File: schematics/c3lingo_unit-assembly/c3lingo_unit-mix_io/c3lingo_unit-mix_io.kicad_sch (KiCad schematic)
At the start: 42 parts, among them J201 Stage Line-In, J202 Mix Line-Out, J203 PowerSupply, J204 Inputs, J205 Output, U201 LM833N, U202 DRV134PA, U203 LM833N

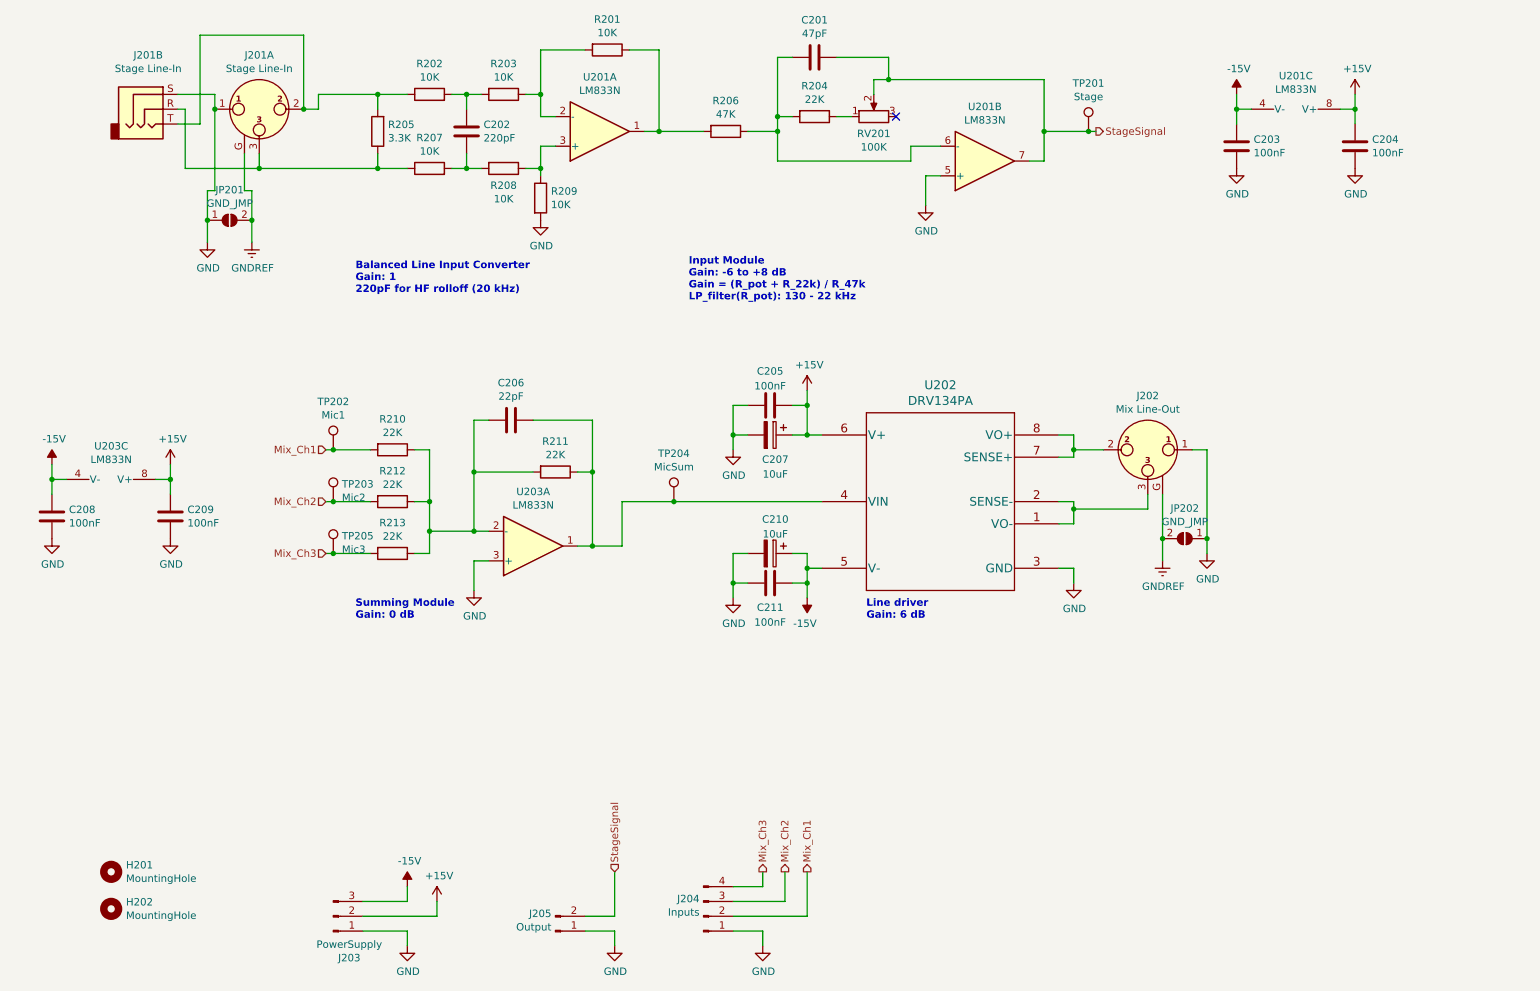
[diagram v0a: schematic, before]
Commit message: Reworks board-to-board connections
Instead of having connections between all boards, use the mix_io board as an audio signal distribution hub.

Note: PCB not updated
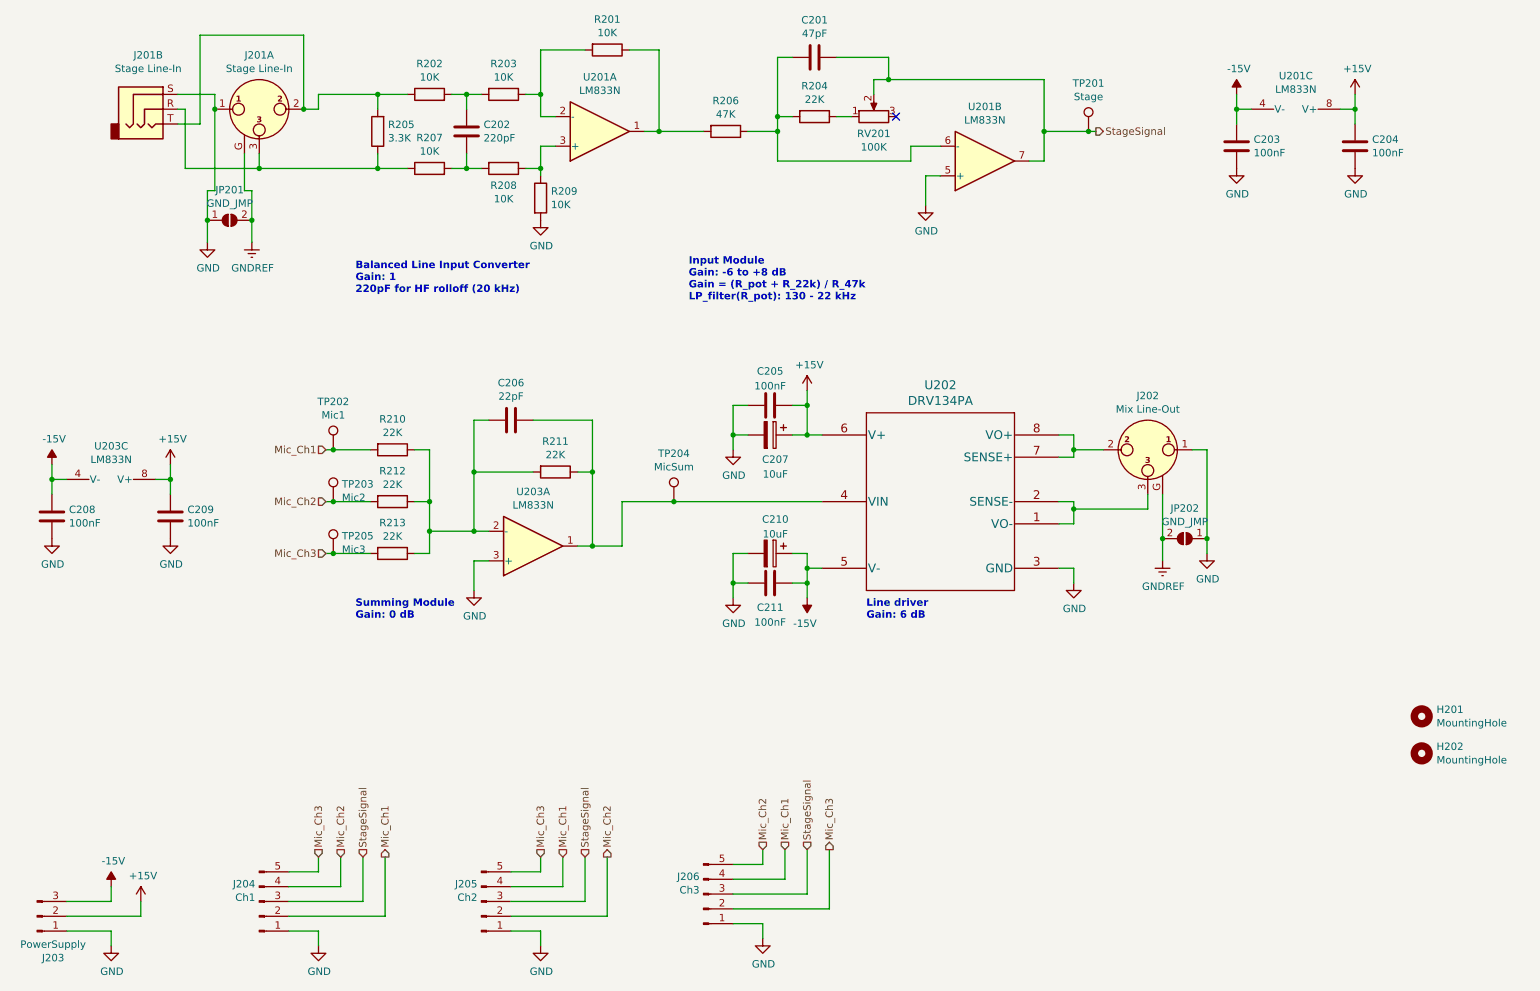
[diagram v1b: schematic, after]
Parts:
- removed J205: Output, TerminalBlock_Phoenix:TerminalBlock_Phoenix_PTSM-0,5-2-2.5-V-THR_1x02_P2.50mm_Vertical, symbol Connector:Conn_01x02_Pin
- added J205: Ch2, TerminalBlock_Phoenix:TerminalBlock_Phoenix_PTSM-0,5-5-2.5-V-THR_1x05_P2.50mm_Vertical, symbol Connector:Conn_01x05_Pin
- added J206: Ch3, TerminalBlock_Phoenix:TerminalBlock_Phoenix_PTSM-0,5-5-2.5-V-THR_1x05_P2.50mm_Vertical, symbol Connector:Conn_01x05_Pin
- J203: footprint TerminalBlock_Phoenix:TerminalBlock_Phoenix_PTSM-0,5-3-2.5-H-THR_1x03_P2.50mm_Horizontal -> TerminalBlock_Phoenix:TerminalBlock_Phoenix_PTSM-0,5-3-2.5-V-THR_1x03_P2.50mm_Vertical
- J204: value Inputs -> Ch1; footprint TerminalBlock_Phoenix:TerminalBlock_Phoenix_PTSM-0,5-4-2.5-V-THR_1x04_P2.50mm_Vertical -> TerminalBlock_Phoenix:TerminalBlock_Phoenix_PTSM-0,5-5-2.5-V-THR_1x05_P2.50mm_Vertical; symbol Connector:Conn_01x04_Pin -> Connector:Conn_01x05_Pin; Model PTSM 0,5/ 4-2,5-V THR -> PTSM 0,5/ 5-2,5-V THR
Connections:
- net GND: now also J205.1 (Pin_1), J206.1 (Pin_1)
- net StageSignal: now also J204.3 (Pin_3), J205.3 (Pin_3), J206.3 (Pin_3)
- net Mix_Ch1 renamed Mic_Ch1
- net Mic_Ch1: now also J205.4 (Pin_4), J206.4 (Pin_4)
- net Mix_Ch2 renamed Mic_Ch2
- net Mic_Ch2: now also J204.4 (Pin_4), J205.2 (Pin_2), J206.5 (Pin_5); no longer J204.3 (Pin_3)
- net Mix_Ch3 renamed Mic_Ch3
- net Mic_Ch3: now also J204.5 (Pin_5), J205.5 (Pin_5), J206.2 (Pin_2); no longer J204.4 (Pin_4)
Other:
- moved on the sheet: H201, H202, J203

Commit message: Re-layout boards with SMD components
* Channel Mix: Removed vu meter potentiometer as good setting was found (10 dB
  more headroom)
* Channel Mix: Add vu meter alternate power
* Channel I/O: Added jumper for phantom power enable/disable
* Add GND test points
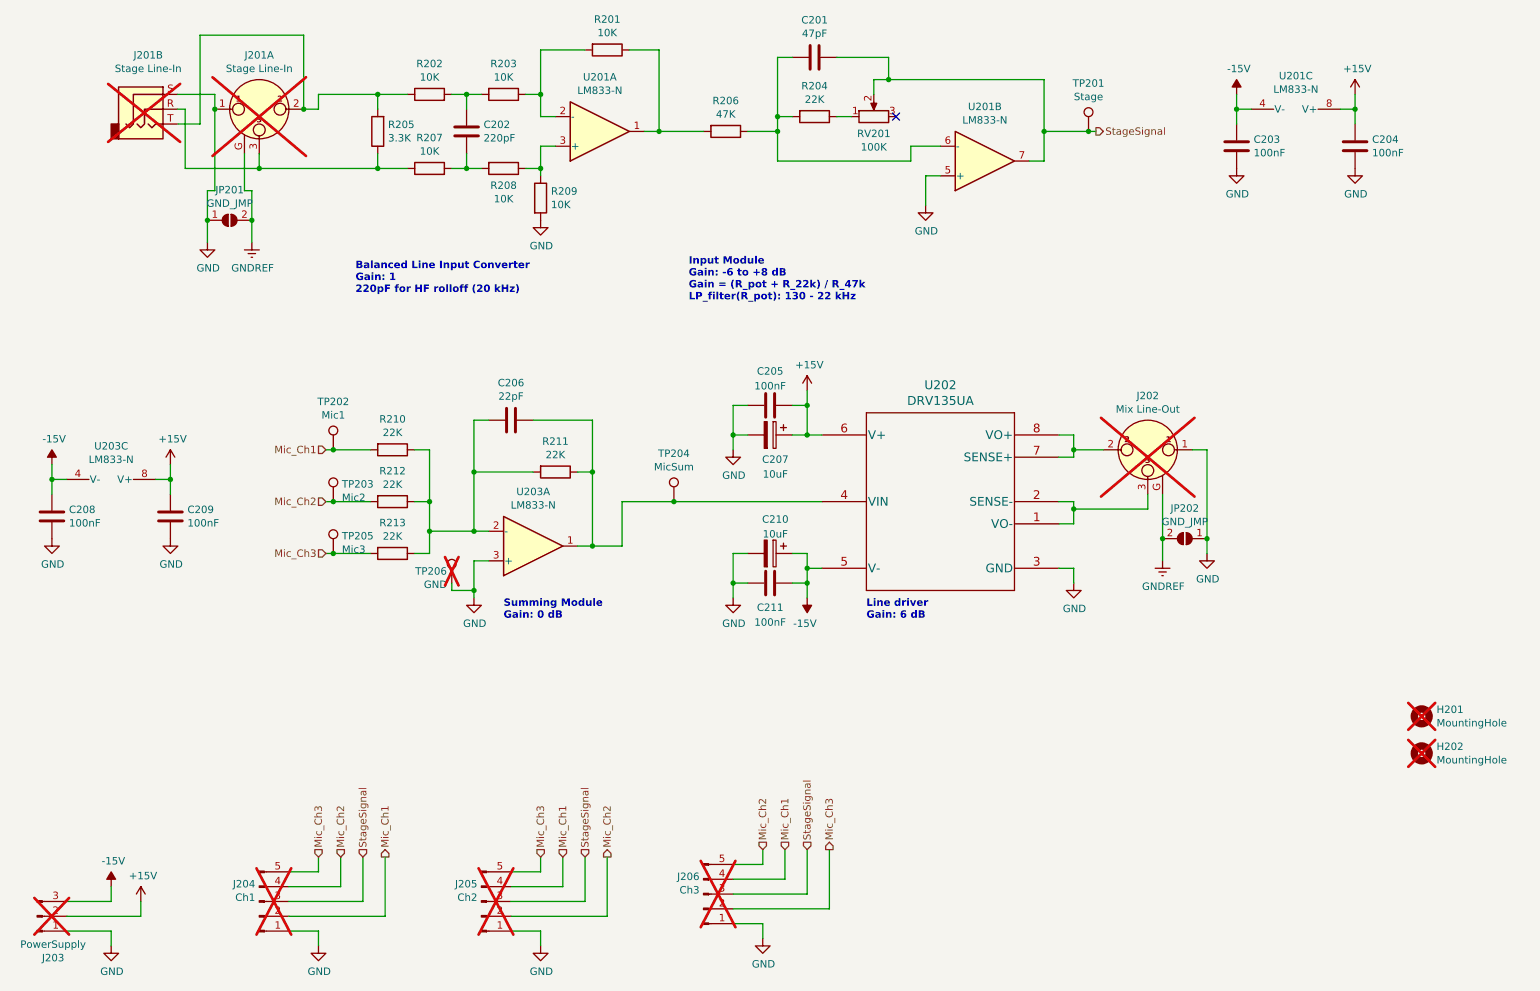
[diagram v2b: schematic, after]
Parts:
- added TP206: GND, TestPoint:TestPoint_Keystone_5005-5009_Compact, symbol Connector:TestPoint
- C201: footprint Capacitor_THT:C_Disc_D5.0mm_W2.5mm_P5.00mm -> Capacitor_SMD:C_0603_1608Metric_Pad1.08x0.95mm_HandSolder; LCSC Part # (none) -> C1671; Model (none) -> 5% C0G
- C202: footprint Capacitor_THT:C_Disc_D5.0mm_W2.5mm_P5.00mm -> Capacitor_SMD:C_0603_1608Metric_Pad1.08x0.95mm_HandSolder; LCSC Part # (none) -> C1603; Model (none) -> 5% C0G
- C203, C204, C205, C208, C209, C211: footprint Capacitor_THT:C_Disc_D5.0mm_W2.5mm_P5.00mm -> Capacitor_SMD:C_0603_1608Metric_Pad1.08x0.95mm_HandSolder; LCSC Part # (none) -> C14663; Model (none) -> 10% X7R 25V+
- C206: footprint Capacitor_THT:C_Disc_D5.0mm_W2.5mm_P5.00mm -> Capacitor_SMD:C_0603_1608Metric_Pad1.08x0.95mm_HandSolder; LCSC Part # (none) -> C1653; Model (none) -> 5% C0G
- C207, C210: footprint Capacitor_THT:CP_Radial_D5.0mm_P2.00mm -> Capacitor_SMD:C_Elec_4x5.4; LCSC Part # (none) -> C3001226; Model (none) -> 25V+
- H201, H202: now not fitted; now left out of the parts list
- J201, J202, J204, J205, J206: now not fitted
- J203: Model PTSM 0,5/ 3-2,5-H THR -> PTSM 0,5/ 3-2,5-V THR; now not fitted
- JP201, JP202, TP201, TP202, TP203, TP204, TP205: now left out of the parts list
- R201, R202, R203, R207, R208, R209: footprint Resistor_THT:R_Axial_DIN0207_L6.3mm_D2.5mm_P10.16mm_Horizontal -> Resistor_SMD:R_0805_2012Metric_Pad1.20x1.40mm_HandSolder; LCSC Part # (none) -> C17414
- R204, R210, R211, R212, R213: footprint Resistor_THT:R_Axial_DIN0207_L6.3mm_D2.5mm_P10.16mm_Horizontal -> Resistor_SMD:R_0805_2012Metric_Pad1.20x1.40mm_HandSolder; LCSC Part # (none) -> C17560
- R205: footprint Resistor_THT:R_Axial_DIN0207_L6.3mm_D2.5mm_P10.16mm_Horizontal -> Resistor_SMD:R_0805_2012Metric_Pad1.20x1.40mm_HandSolder; LCSC Part # (none) -> C26010
- R206: footprint Resistor_THT:R_Axial_DIN0207_L6.3mm_D2.5mm_P10.16mm_Horizontal -> Resistor_SMD:R_0805_2012Metric_Pad1.20x1.40mm_HandSolder; LCSC Part # (none) -> C17713
- RV201: Model Vishay M64Y104 -> Bourns PV36Y104C01B00 or Vishay M64Y104
- U201, U203: value LM833N -> LM833-N; footprint Package_DIP:DIP-8_W7.62mm_Socket_LongPads -> Package_SO:SOIC-8_3.9x4.9mm_P1.27mm; LCSC Part # (none) -> C473907; Model +DIP-8 Socket -> LM833M or LM833MX (SOIC-8)
- U202: value DRV134PA -> DRV135UA; footprint Package_DIP:DIP-8_W7.62mm -> Package_SO:SOIC-8_3.9x4.9mm_P1.27mm; symbol JBeyerstedt-Library:DRV134PA -> c3lingo_unit:DRV134PA; LCSC Part # (none) -> C431073; Model +DIP-8 Socket -> DRV135UA (SOIC-8)
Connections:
- net GND: now also TP206.1

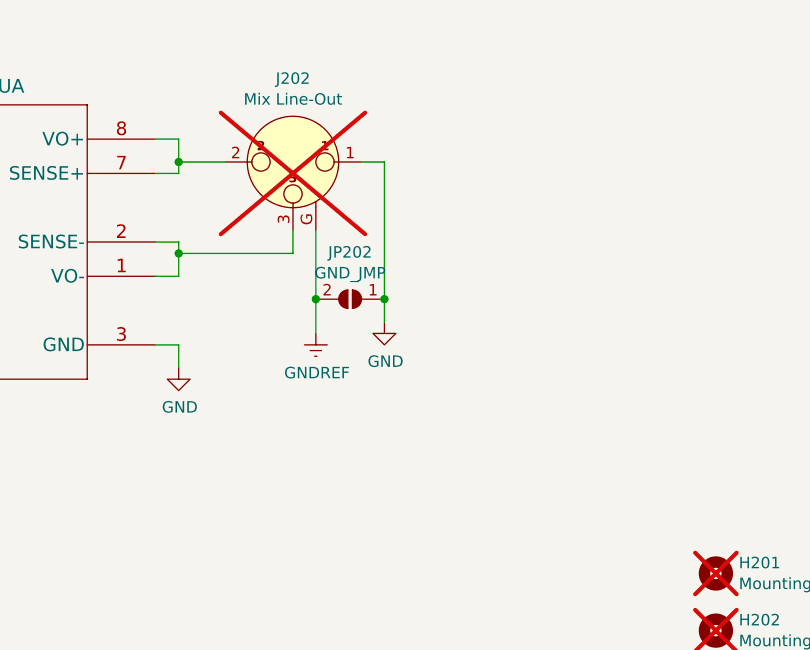
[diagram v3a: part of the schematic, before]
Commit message: Mix I/O: Add ground lift
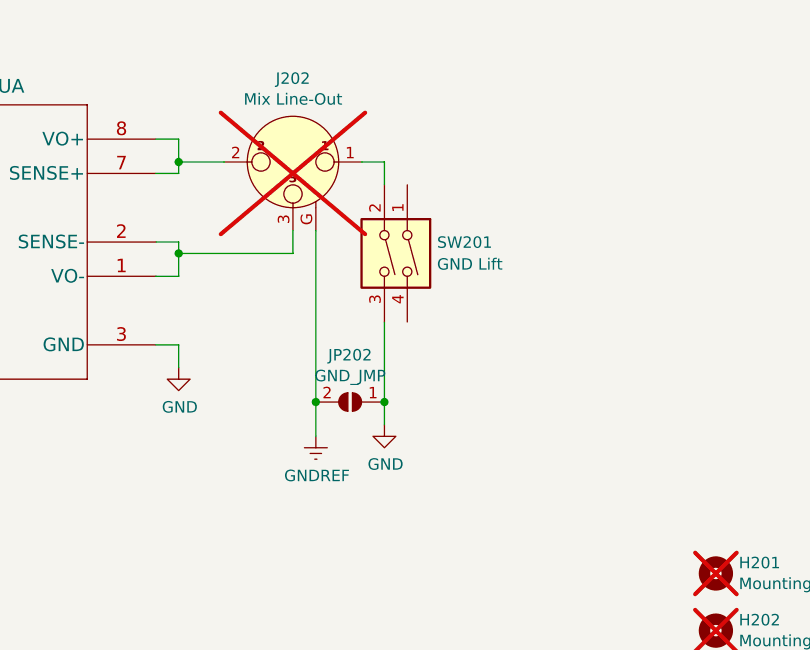
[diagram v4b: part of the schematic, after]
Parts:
- added SW201: GND Lift, Button_Switch_THT:SW_DIP_SPSTx02_Piano_CTS_Series194-2MSTN_W7.62mm_P2.54mm, symbol Switch:SW_DIP_x02
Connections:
- net GND: now also SW201.3; no longer J202.1
- new net: J202.1, SW201.2
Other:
- moved on the sheet: JP202
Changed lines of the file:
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@@
 	(title_block
 		(title "c3lingo interpeter unit -- mix and line I/O")
-		(date "2024-07-07")
-		(rev "v0.3.0")
+		(date "2024-07-08")
+		(rev "v0.3.1")
 		(company "Jannik Beyerstedt (jtbx)")
 		(comment 1 "Prototype 2")
@@
 	)
 	(junction
-		(at 226.06 120.65)
+		(at 226.06 132.08)
 		(diameter 0)
 		(color 0 0 0 0)
@@
 	)
 	(junction
-		(at 218.44 120.65)
+		(at 218.44 132.08)
 		(diameter 0)
 		(color 0 0 0 0)
@@
 	(wire
 		(pts
-			(xy 218.44 113.03) (xy 218.44 120.65)
+			(xy 218.44 113.03) (xy 218.44 132.08)
 		)
 		(stroke
@@
 	(wire
 		(pts
-			(xy 226.06 105.41) (xy 226.06 120.65)
+			(xy 226.06 105.41) (xy 226.06 107.95)
 		)
 		(stroke
@@
 	(wire
 		(pts
-			(xy 226.06 120.65) (xy 226.06 123.19)
+			(xy 226.06 132.08) (xy 226.06 134.62)
 		)
 		(stroke
@@
 	(wire
 		(pts
-			(xy 218.44 120.65) (xy 218.44 124.46)
+			(xy 218.44 132.08) (xy 218.44 135.89)
 		)
 		(stroke
@@
 	(wire
 		(pts
+			(xy 226.06 123.19) (xy 226.06 132.08)
+		)
+		(stroke
+			(width 0)
+			(type default)
+		)
+	)
+	(wire
+		(pts
 			(xy 30.48 185.42) (xy 43.18 185.42)
 		)
@@
 	(symbol
 		(lib_id "power:GND")
-		(at 226.06 123.19 0)
+		(at 226.06 134.62 0)
 		(unit 1)
 		(exclude_from_sim no)
@@
 		(dnp no)
 		(property "Reference" "#PWR0215"
-			(at 226.06 129.54 0)
+			(at 226.06 140.97 0)
 			(effects
 				(font
@@
 		)
 		(property "Value" "GND"
-			(at 226.187 127.5842 0)
+			(at 226.187 139.0142 0)
 			(effects
 				(font
@@
 		)
 		(property "Footprint" ""
-			(at 226.06 123.19 0)
+			(at 226.06 134.62 0)
 			(effects
 				(font
@@
 		)
 		(property "Datasheet" ""
-			(at 226.06 123.19 0)
+			(at 226.06 134.62 0)
 			(effects
 				(font
@@
 		)
 		(property "Description" "Power symbol creates a global label with name \"GND\" , ground"
-			(at 226.06 123.19 0)
+			(at 226.06 134.62 0)
 			(effects
 				(font
@@
 	(symbol
 		(lib_id "Jumper:SolderJumper_2_Open")
-		(at 222.25 120.65 0)
+		(at 222.25 132.08 0)
 		(mirror y)
 		(unit 1)
@@
 		(dnp no)
 		(property "Reference" "JP202"
-			(at 222.25 115.443 0)
+			(at 222.25 126.873 0)
 			(effects
 				(font
@@
 		)
 		(property "Value" "GND_JMP"
-			(at 222.25 117.7544 0)
+			(at 222.25 129.1844 0)
 			(effects
 				(font
@@
 		)
 		(property "Footprint" "Jumper:SolderJumper-2_P1.3mm_Open_TrianglePad1.0x1.5mm"
-			(at 222.25 120.65 0)
+			(at 222.25 132.08 0)
 			(effects
 				(font
@@
 		)
 		(property "Datasheet" "~"
-			(at 222.25 120.65 0)
+			(at 222.25 132.08 0)
 			(effects
 				(font
@@
 		)
 		(property "Description" ""
-			(at 222.25 120.65 0)
+			(at 222.25 132.08 0)
 			(effects
 				(font
@@
 		)
 		(property "LCSC Part #" ""
-			(at 222.25 120.65 0)
+			(at 222.25 132.08 0)
 			(effects
 				(font
@@
 	(symbol
 		(lib_id "power:GNDREF")
-		(at 218.44 124.46 0)
+		(at 218.44 135.89 0)
 		(unit 1)
 		(exclude_from_sim no)
@@
 		(dnp no)
 		(property "Reference" "#PWR0216"
-			(at 218.44 130.81 0)
+			(at 218.44 142.24 0)
 			(effects
 				(font
@@
 		)
 		(property "Value" "GNDREF"
-			(at 218.567 128.8542 0)
+			(at 218.567 140.2842 0)
 			(effects
 				(font
@@
 		)
 		(property "Footprint" ""
-			(at 218.44 124.46 0)
+			(at 218.44 135.89 0)
 			(effects
 				(font
@@
 		)
 		(property "Datasheet" ""
-			(at 218.44 124.46 0)
+			(at 218.44 135.89 0)
 			(effects
 				(font
@@
 		)
 		(property "Description" "Power symbol creates a global label with name \"GNDREF\" , reference supply ground"
-			(at 218.44 124.46 0)
+			(at 218.44 135.89 0)
 			(effects
 				(font
@@
 					(unit 1)
 				)
+			)
+		)
+	)
+	(symbol
+		(lib_id "Switch:SW_DIP_x02")
+		(at 226.06 115.57 270)
+		(unit 1)
+		(exclude_from_sim no)
+		(in_bom yes)
+		(on_board yes)
+		(dnp no)
+		(fields_autoplaced yes)
+		(property "Reference" "SW201"
+			(at 231.902 114.3578 90)
+			(effects
+				(font
+					(size 1.27 1.27)
+				)
+				(justify left)
+			)
+		)
+		(property "Value" "GND Lift"
+			(at 231.902 116.7821 90)
+			(effects
+				(font
+					(size 1.27 1.27)
+				)
+				(justify left)
+			)
+		)
+		(property "Footprint" "Button_Switch_THT:SW_DIP_SPSTx02_Piano_CTS_Series194-2MSTN_W7.62mm_P2.54mm"
+			(at 226.06 115.57 0)
+			(effects
+				(font
+					(size 1.27 1.27)
+				)
+				(hide yes)
+			)
+		)
+		(property "Datasheet" "~"
+			(at 226.06 115.57 0)
+			(effects
+				(font
+					(size 1.27 1.27)
+				)
+				(hide yes)
+			)
+		)
+		(property "Description" "CTS 195-2MST"
+			(at 226.06 115.57 0)
+			(effects
+				(font
+					(size 1.27 1.27)
+				)
+				(hide yes)
+			)
+		)
+		(pin "1"
+		)
+		(pin "2"
+		)
+		(pin "4"
+		)
+		(pin "3"
+		)
+		(instances
+			(project ""
+				(path "/21e9fedd-b749-4b85-a03a-dffb926d039f"
+					(reference "SW201")
+					(unit 1)
+				)
+			)
+			(project ""
+				(path "/9e80d1ee-62c1-483d-830d-f559e7294d20/00000000-0000-0000-0000-000060ae0dae"
+					(reference "SW201")
+					(unit 1)
+				)
